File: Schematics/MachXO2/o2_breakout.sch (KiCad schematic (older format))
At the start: 34 parts, among them J1 Conn_02x20_Odd_Even, J2 Conn_02x20_Odd_Even, SW3 Reset, U1 LCMXO2-2000HC-4TG100C, U3 TCM809, U5 CY7C1010, U8 74AHC1G08, X1 19.6608MHz

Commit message: Update Schematic
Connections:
- wire segments 361 -> 363
- no-connect marks 28 -> 27
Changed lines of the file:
@@
 	10500 4250 10700 4250
 Wire Wire Line
-	10500 5550 10750 5550
+	10500 5450 10750 5450
 Text Label 10700 4250 2    50   ~ 0
 clkE
@@
 Text Label 5600 6400 2    50   ~ 0
 ~RTS
-Text Label 10750 5550 2    50   ~ 0
+Text Label 10750 5450 2    50   ~ 0
 GCLK1
 Text Label 5600 5200 2    50   ~ 0
@@
 Wire Wire Line
 	9700 5650 10000 5650
-Wire Wire Line
-	10500 5650 10800 5650
-Text Label 10800 5650 2    50   ~ 0
+Text Label 11050 5650 2    50   ~ 0
 SPI_CS3
 NoConn ~ 10000 5750
@@
 NoConn ~ 10500 5250
 NoConn ~ 10500 5350
-NoConn ~ 10500 5450
 NoConn ~ 10500 5750
 NoConn ~ 10000 1850
@@
 Wire Wire Line
 	9650 5950 9650 5050
-Wire Wire Line
-	10500 5950 10700 5950
 Wire Wire Line
 	10700 5950 10700 6050
@@
 L power:+5V #PWR?
 U 1 1 6089F76D
-P 10900 5750
+P 10900 5800
 AR Path="/5E6A6650/6089F76D" Ref="#PWR?"  Part="1"
 AR Path="/6089F76D" Ref="#PWR0107"  Part="1"
-F 0 "#PWR0107" H 10900 5600 50  0001 C CNN
-F 1 "+5V" H 10915 5923 50  0000 C CNN
-F 2 "" H 10900 5750 50  0001 C CNN
-F 3 "" H 10900 5750 50  0001 C CNN
-	1    10900 5750
-	1    0    0    -1
-$EndComp
-Wire Wire Line
-	10900 5750 10900 5850
+F 0 "#PWR0107" H 10900 5650 50  0001 C CNN
+F 1 "+5V" H 11000 5900 50  0000 C CNN
+F 2 "" H 10900 5800 50  0001 C CNN
+F 3 "" H 10900 5800 50  0001 C CNN
+	1    10900 5800
+	1    0    0    -1
+$EndComp
+Wire Wire Line
+	10900 5800 10900 5850
 Wire Wire Line
 	10500 5850 10900 5850
@@
 	10500 4850 10700 4850
 Wire Wire Line
-	11050 4650 11050 6150
-Wire Wire Line
-	11050 6150 10700 6150
-Wire Wire Line
-	10500 4650 11050 4650
+	11100 4650 11100 6150
+Wire Wire Line
+	11100 6150 10700 6150
+Wire Wire Line
+	10500 4650 11100 4650
 Connection ~ 10700 6150
 Wire Wire Line
@@
 Text Label 5600 4900 2    50   ~ 0
 nCS2
+Wire Wire Line
+	10500 5550 10700 5550
+Wire Wire Line
+	10700 5550 10700 5950
+Wire Wire Line
+	10500 5950 10700 5950
+Connection ~ 10700 5950
+Wire Wire Line
+	10500 5650 11050 5650
 Wire Bus Line
 	8000 1200 8000 3100

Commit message: Add schematic Rev C3.
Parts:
- added R12: 10K, Capacitors_SMD:C_0402, symbol CPU2908CLocal:R
- SW3: symbol Switch:SW_DPST_x2 -> o2_breakout-rescue:SW_DPST_x2-Switch
- U1: symbol FPGA_Lattice:LCMXO2-2000HC-4TG100C -> o2_breakout-rescue:LCMXO2-2000HC-4TG100C-FPGA_Lattice
- X1: symbol Oscillator:SG-8002CA -> o2_breakout-rescue:SG-8002CA-Oscillator
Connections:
- net labels added: FT_Reset
- wire segments 363 -> 368
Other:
- moved on the sheet: U3
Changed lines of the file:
@@
 L power:GND #PWR09
 U 1 1 5DC5EC0E
-P 9150 2100
-F 0 "#PWR09" H 9150 1850 50  0001 C CNN
-F 1 "GND" H 9155 1927 50  0000 C CNN
-F 2 "" H 9150 2100 50  0001 C CNN
-F 3 "" H 9150 2100 50  0001 C CNN
-	1    9150 2100
-	1    0    0    -1
-$EndComp
-Wire Wire Line
-	9150 1950 9150 2000
+P 8850 2100
+F 0 "#PWR09" H 8850 1850 50  0001 C CNN
+F 1 "GND" H 8855 1927 50  0000 C CNN
+F 2 "" H 8850 2100 50  0001 C CNN
+F 3 "" H 8850 2100 50  0001 C CNN
+	1    8850 2100
+	1    0    0    -1
+$EndComp
+Wire Wire Line
+	8850 1950 8850 2000
 Wire Wire Line
 	9650 6050 9650 6150
 $Comp
-L Oscillator:SG-8002CA X1
+L o2_breakout-rescue:SG-8002CA-Oscillator X1
 U 1 1 5DCCEBCB
 P 6450 5800
@@
 L Power_Supervisor:TCM809 U3
 U 1 1 5DC41577
-P 9250 1550
-F 0 "U3" H 9020 1596 50  0000 R CNN
-F 1 "TCM809" H 9020 1505 50  0000 R CNN
-F 2 "digikey-footprints:SOT-23-3" H 8850 1700 50  0001 C CNN
-F 3 "http://ww1.microchip.com/downloads/en/DeviceDoc/21661E.pdf" H 8950 1800 50  0001 C CNN
-	1    9250 1550
+P 8950 1550
+F 0 "U3" H 8720 1596 50  0000 R CNN
+F 1 "TCM809" H 8720 1505 50  0000 R CNN
+F 2 "digikey-footprints:SOT-23-3" H 8550 1700 50  0001 C CNN
+F 3 "http://ww1.microchip.com/downloads/en/DeviceDoc/21661E.pdf" H 8650 1800 50  0001 C CNN
+	1    8950 1550
 	1    0    0    -1
 $EndComp
@@
 $EndComp
 $Comp
-L power:+3V6 #PWR?
+L o2_breakout-rescue:+3V6-power #PWR?
 U 1 1 5DE300A4
 P 9350 900
@@
 Text Label 10500 1450 2    50   ~ 0
 nReset
-Text Label 8950 4850 0    50   ~ 0
-nReset
-Wire Wire Line
-	8950 4850 8850 4850
 $Comp
 L sram:CY7C1010 U5
@@
 Connection ~ 5850 7050
 $Comp
-L Switch:SW_DPST_x2 SW3
+L o2_breakout-rescue:SW_DPST_x2-Switch SW3
 U 1 1 5DEE7A37
 P 8250 1300
@@
 SPI_CLK
 Wire Wire Line
-	9950 1350 9950 1100
+	9950 1350 9950 1150
 Text Label 1800 4100 0    50   ~ 0
 clkE
@@
 	2150 4700 2150 5800
 $Comp
-L FPGA_Lattice:LCMXO2-2000HC-4TG100C U1
+L o2_breakout-rescue:LCMXO2-2000HC-4TG100C-FPGA_Lattice U1
 U 1 1 5DC03110
 P 2300 1500
@@
 	8250 1100 8500 1100
 Wire Wire Line
-	9550 1550 9600 1550
-Wire Wire Line
 	9600 1400 9600 1550
 Wire Wire Line
-	8500 700  9150 700
-Wire Wire Line
-	9150 700  9150 1150
+	8500 700  8850 700
+Wire Wire Line
+	8850 700  8850 1150
 Connection ~ 8500 700
-Wire Wire Line
-	8500 2000 9150 2000
-Connection ~ 9150 2000
-Wire Wire Line
-	9150 2000 9150 2100
+Connection ~ 8850 2000
+Wire Wire Line
+	8850 2000 8850 2100
 Connection ~ 6200 7050
 Connection ~ 6200 7500
@@
 Wire Wire Line
 	10500 5650 11050 5650
+Wire Wire Line
+	8500 2000 8850 2000
+Wire Wire Line
+	9250 1550 9350 1550
+Text Label 9300 1550 0    50   ~ 0
+FT_Reset
+Text Label 9350 4850 2    50   ~ 0
+FT_Reset
+Wire Wire Line
+	8850 4850 9350 4850
+$Comp
+L CPU2908CLocal:R R?
+U 1 1 5E34444C
+P 9350 1350
+AR Path="/5E6A6650/5E34444C" Ref="R?"  Part="1"
+AR Path="/5E34444C" Ref="R12"  Part="1"
+F 0 "R12" H 9420 1396 50  0000 L CNN
+F 1 "10K" H 9420 1305 50  0000 L CNN
+F 2 "Capacitors_SMD:C_0402" V 9280 1350 50  0001 C CNN
+F 3 "~" H 9350 1350 50  0001 C CNN
+	1    9350 1350
+	1    0    0    -1
+$EndComp
+Wire Wire Line
+	9350 1500 9350 1550
+Connection ~ 9350 1550
+Wire Wire Line
+	9350 1550 9600 1550
+Wire Wire Line
+	9350 1200 9350 1150
+Wire Wire Line
+	9350 1150 9950 1150
 Wire Bus Line
 	8000 1200 8000 3100
@@
 Wire Bus Line
 	6050 1100 6050 3500
+Connection ~ 9950 1150
+Wire Wire Line
+	9950 1150 9950 1100
 $EndSCHEMATC

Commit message: Update BreakOut Schematic.
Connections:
- net +3V3: no longer J1.2 (Pin_2)
- net GND: now also J1.2 (Pin_2), J1.20 (Pin_20)
- net ~SD_CD: now also U1.62 (PR7B)
- no-connect marks 27 -> 24
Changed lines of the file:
@@
 UM4
 Wire Wire Line
-	10950 5150 10950 4150
-Wire Wire Line
 	10950 2850 10950 3950
-Connection ~ 10950 4150
 Wire Wire Line
 	10950 1850 10950 2750
@@
 Wire Wire Line
 	10500 2850 10950 2850
-Wire Wire Line
-	10500 4150 10950 4150
 Wire Wire Line
 	10500 5150 10950 5150
@@
 NoConn ~ 10500 5350
 NoConn ~ 10500 5750
-NoConn ~ 10000 1850
 NoConn ~ 10000 2050
 NoConn ~ 10000 2150
@@
 Wire Wire Line
 	10850 3750 10850 3650
-NoConn ~ 10500 5050
 NoConn ~ 2300 3500
 NoConn ~ 2300 3100
@@
 NoConn ~ 2300 4300
 NoConn ~ 5100 4800
-NoConn ~ 5100 5300
 NoConn ~ 2300 5700
 NoConn ~ 2300 5900
@@
 Connection ~ 10950 3950
 Wire Wire Line
-	10950 3950 10950 4150
-Wire Wire Line
 	10000 1850 9850 1850
 Wire Wire Line
@@
 	10500 4850 10700 4850
 Wire Wire Line
-	11100 4650 11100 6150
+	11100 4650 11100 5050
 Wire Wire Line
 	11100 6150 10700 6150
@@
 Wire Wire Line
 	9250 1550 9350 1550
-Text Label 9300 1550 0    50   ~ 0
+Text Label 9700 1700 2    50   ~ 0
 FT_Reset
 Text Label 9350 4850 2    50   ~ 0
@@
 Wire Wire Line
 	9350 1150 9950 1150
+Connection ~ 9950 1150
+Wire Wire Line
+	9950 1150 9950 1100
+Wire Wire Line
+	9350 1550 9350 1700
+Wire Wire Line
+	9350 1700 9700 1700
+Wire Wire Line
+	5100 5300 5600 5300
+Text Label 5600 5300 2    50   ~ 0
+~SD_CD
+Wire Wire Line
+	10950 3950 10950 5150
+Wire Wire Line
+	10500 4150 11100 4150
+Wire Wire Line
+	11100 4150 11100 4650
+Connection ~ 11100 4650
+Wire Wire Line
+	10500 5050 11100 5050
 Wire Bus Line
 	8000 1200 8000 3100
@@
 Wire Bus Line
 	6050 1100 6050 3500
-Connection ~ 9950 1150
-Wire Wire Line
-	9950 1150 9950 1100
+Connection ~ 11100 5050
+Wire Wire Line
+	11100 5050 11100 6150
 $EndSCHEMATC

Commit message: Update Schematics
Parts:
- added C38: 0.1uF, Capacitors_SMD:C_0402, symbol Device:C
- added R26: 10K, Capacitors_SMD:C_0402, symbol CPU2908CLocal:R
- added SW1: USER, Buttons_Switches_ThroughHole:SW_PUSH_6mm, symbol o2_breakout-rescue:SW_DPST_x2-Switch
- added unit 1 of SW2
- renumbered SW3 to SW2
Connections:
- net +3V3: now also R26.1; no longer J2.20 (Pin_20), J2.22 (Pin_22)
- net A0: now also J2.8 (Pin_8); no longer J2.10 (Pin_10)
- net A1: now also J2.7 (Pin_7); no longer J2.9 (Pin_9)
- net A10: now also J2.20 (Pin_20); no longer J2.26 (Pin_26)
- net A11: now also J2.19 (Pin_19); no longer J2.25 (Pin_25)
- net A12: now also J2.22 (Pin_22); no longer J2.28 (Pin_28)
- net A13: now also J2.21 (Pin_21); no longer J2.27 (Pin_27)
- net A14: now also J2.24 (Pin_24); no longer J2.30 (Pin_30)
- net A15: now also J2.23 (Pin_23); no longer J2.29 (Pin_29)
- net A16: now also J2.28 (Pin_28); no longer J2.32 (Pin_32)
- net A17: now also J2.27 (Pin_27); no longer J2.31 (Pin_31)
- net A18: now also J2.30 (Pin_30); no longer J2.34 (Pin_34)
- net A19: now also J2.29 (Pin_29); no longer J2.33 (Pin_33)
- net A2: now also J2.10 (Pin_10); no longer J2.12 (Pin_12)
- net A3: now also J2.9 (Pin_9); no longer J2.11 (Pin_11)
- net A4: now also J2.12 (Pin_12); no longer J2.14 (Pin_14)
- net A5: now also J2.11 (Pin_11); no longer J2.13 (Pin_13)
- net A6: now also J2.14 (Pin_14); no longer J2.16 (Pin_16)
- net A7: now also J2.13 (Pin_13); no longer J2.15 (Pin_15)
- net A8: now also J2.18 (Pin_18); no longer J2.24 (Pin_24)
- net A9: now also J2.17 (Pin_17); no longer J2.23 (Pin_23)
- net GND: now also J1.13 (Pin_13), J1.14 (Pin_14), J2.15 (Pin_15), J2.16 (Pin_16), J2.25 (Pin_25), J2.26 (Pin_26), J2.31 (Pin_31), J2.32 (Pin_32), SW2.4 (B), C38.2, SW1.1 (A), SW1.4 (B), SW2.1 (A); no longer J1.12 (Pin_12), J1.19 (Pin_19), J1.20 (Pin_20), J2.19 (Pin_19), J2.21 (Pin_21), J2.37 (Pin_37), J2.38 (Pin_38), J2.39 (Pin_39), J2.40 (Pin_40), SW2.1 (A)
- net IO0: now also J2.34 (Pin_34)
- net IO1: now also J2.33 (Pin_33)
- net IO2: now also J2.36 (Pin_36)
- net IO3: now also J2.35 (Pin_35)
- net IO4: now also J2.38 (Pin_38)
- net IO5: now also J2.37 (Pin_37)
- net IO6: now also J2.40 (Pin_40)
- net IO7: now also J2.39 (Pin_39)
- net ~SD_CD: now also J2.5 (Pin_5); no longer J2.8 (Pin_8)
- net ~nAltRD: now also J1.20 (Pin_20); no longer J1.17 (Pin_17)
- net ~nAltWR: now also J1.19 (Pin_19); no longer J1.18 (Pin_18)
- net USER: now reaches U1.15 (PL9B)
- net USER: now also C38.1, R26.2, SW1.3 (A)
- net ~CS1: now reaches U1.29 (PB6A)
- net ~CS1: now also J1.8 (Pin_8)
- net at C26.1, U8.2: now also SW2.3 (A); no longer R10.2, SW2.2 (B)
- net UM0 renamed IO8
- net IO8: now also J1.10 (Pin_10); no longer J1.8 (Pin_8)
- net UM1 renamed IO9
- net UM2 renamed IO10
- net IO10: now also J1.12 (Pin_12); no longer J1.10 (Pin_10)
- net UM3 renamed IO11
- net UM4 renamed IO12
- net IO12: now also J1.16 (Pin_16); no longer J1.13 (Pin_13)
- net UM5 renamed IO13
- net IO13: now also J1.15 (Pin_15); no longer J1.14 (Pin_14)
- net UM6 renamed IO14
- net IO14: now also J1.18 (Pin_18); no longer J1.15 (Pin_15)
- net UM7 renamed IO15
- net IO15: now also J1.17 (Pin_17); no longer J1.16 (Pin_16)
- net nCS0 renamed ~CE
- net nCS2 renamed ~CS2
- new net: R10.2, SW2.2 (B)
- no-connect marks 24 -> 17

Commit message: Update schematics
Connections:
- net GND: now also J1.23 (Pin_23), J1.24 (Pin_24)
- no-connect marks 17 -> 15
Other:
- moved on the sheet: C38
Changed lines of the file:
@@
 NoConn ~ 10000 5450
 NoConn ~ 10000 5350
-NoConn ~ 10000 5250
-NoConn ~ 10500 5250
 NoConn ~ 10500 5350
 NoConn ~ 10500 5750
@@
 	10500 4150 11100 4150
 Wire Wire Line
-	7300 4700 7350 4700
+	7300 4700 7450 4700
 $Comp
 L CPU2908CLocal:R R?
@@
 	7200 5250 7200 5350
 Wire Wire Line
-	7350 5250 7200 5250
+	7450 5250 7200 5250
 $Comp
 L o2_breakout-rescue:SW_DPST_x2-Switch SW1
@@
 Connection ~ 9650 4750
 Wire Wire Line
-	9650 4750 9650 5950
+	9650 4750 9650 5250
 Wire Wire Line
 	10950 3950 10950 5150
@@
 Connection ~ 11100 4750
 Wire Wire Line
-	11100 4750 11100 6150
+	11100 4750 11100 5250
 $Comp
 L Connector_Generic:Conn_02x20_Odd_Even J1
@@
 	10500 4450 10700 4450
 Wire Wire Line
-	7350 5150 7350 5250
+	7450 5150 7450 5250
 $Comp
 L Device:C C38
 U 1 1 5E3FD7EE
-P 7350 5000
-F 0 "C38" H 7465 5046 50  0000 L CNN
-F 1 "0.1uF" H 7465 4955 50  0000 L CNN
-F 2 "Capacitors_SMD:C_0402" H 7388 4850 50  0001 C CNN
-F 3 "~" H 7350 5000 50  0001 C CNN
-	1    7350 5000
-	1    0    0    -1
-$EndComp
-Wire Wire Line
-	7350 4700 7350 4850
-Connection ~ 7350 4700
+P 7450 5000
+F 0 "C38" H 7565 5046 50  0000 L CNN
+F 1 "0.1uF" H 7565 4955 50  0000 L CNN
+F 2 "Capacitors_SMD:C_0402" H 7488 4850 50  0001 C CNN
+F 3 "~" H 7450 5000 50  0001 C CNN
+	1    7450 5000
+	1    0    0    -1
+$EndComp
+Wire Wire Line
+	7450 4700 7450 4850
 Text Label 1800 2900 0    50   ~ 0
 USER
 Wire Wire Line
-	7350 4700 7650 4700
-Wire Wire Line
 	1800 2900 2300 2900
+Text Label 6900 4700 0    50   ~ 0
+USER
+Wire Wire Line
+	9650 5250 10000 5250
+Connection ~ 9650 5250
+Wire Wire Line
+	9650 5250 9650 5950
+Wire Wire Line
+	10500 5250 11100 5250
+Connection ~ 11100 5250
+Wire Wire Line
+	11100 5250 11100 6150
+Wire Wire Line
+	6900 4700 7200 4700
+Connection ~ 7200 4700
 Wire Bus Line
 	8000 1200 8000 3100
@@
 Wire Bus Line
 	6050 1100 6050 3500
-Text Label 7650 4700 2    50   ~ 0
-USER
 $EndSCHEMATC

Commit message: Clean up PCB.
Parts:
- removed C26: 0.1uF, Capacitors_SMD:C_0402, symbol Device:C
- added C39: 0.1uF, Capacitors_SMD:C_0402, symbol Device:C
- JP2: footprint Wire_Connections_Bridges:WireConnection_0.80mmDrill -> Wire_Connections_Bridges:WireConnection_1.00mmDrill
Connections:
- net +3V3: now also J1.33 (Pin_33), J1.34 (Pin_34)
- net GND: now also C39.2; no longer J1.37 (Pin_37), J1.38 (Pin_38)
- net at R10.2, SW2.2 (B): now also C39.1
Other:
- moved on the sheet: C1, C2, C3, C35, C4, C5, C6, C7, R10, SW2A

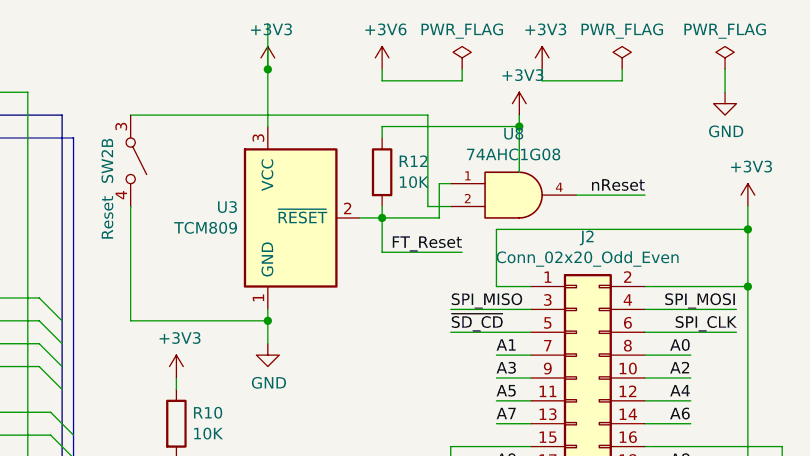
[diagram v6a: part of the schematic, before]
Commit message: asq bug fix.
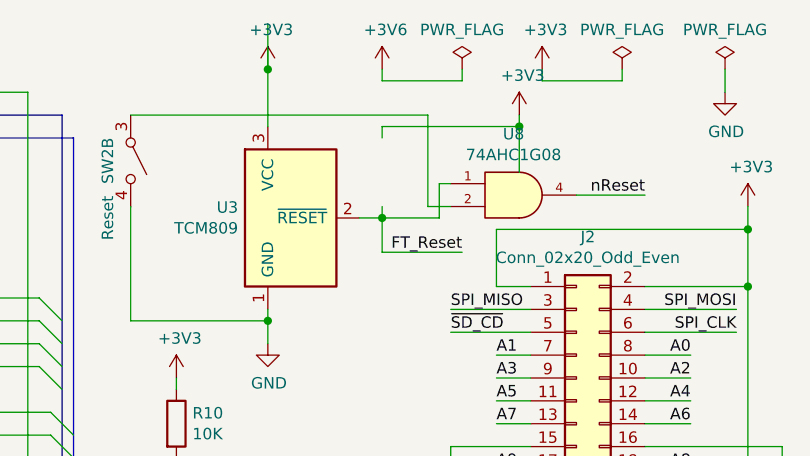
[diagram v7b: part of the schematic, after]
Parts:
- removed R12: 10K, Capacitors_SMD:C_0402, symbol CPU2908CLocal:R
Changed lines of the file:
@@
 Wire Wire Line
 	8850 4850 9350 4850
-$Comp
-L CPU2908CLocal:R R?
-U 1 1 5E34444C
-P 9350 1350
-AR Path="/5E6A6650/5E34444C" Ref="R?"  Part="1"
-AR Path="/5E34444C" Ref="R12"  Part="1"
-F 0 "R12" H 9420 1396 50  0000 L CNN
-F 1 "10K" H 9420 1305 50  0000 L CNN
-F 2 "Capacitors_SMD:C_0402" V 9280 1350 50  0001 C CNN
-F 3 "~" H 9350 1350 50  0001 C CNN
-	1    9350 1350
-	1    0    0    -1
-$EndComp
 Wire Wire Line
 	9350 1500 9350 1550

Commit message: PCB RevA3.
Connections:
- net GND: now also J1.29 (Pin_29)
- net SPI_CS0: now also U1.62 (PR7B); no longer U1.61 (PR9A)
- net ~CS2: now also J1.27 (Pin_27)
- net ~SD_CD: now also U1.61 (PR9A); no longer U1.62 (PR7B)
- no-connect marks 15 -> 13
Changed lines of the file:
@@
 Text Label 5600 5200 2    50   ~ 0
 GCLK1
-Text Label 5600 5100 2    50   ~ 0
-~CS0
 Text Label 5600 5500 2    50   ~ 0
 SPI_CS1
-Text Label 5600 5400 2    50   ~ 0
+Text Label 5600 5300 2    50   ~ 0
 SPI_CS0
 Wire Wire Line
@@
 Text Label 11050 5650 2    50   ~ 0
 SPI_CS3
-NoConn ~ 10000 5550
-NoConn ~ 10000 5450
 NoConn ~ 10000 5350
 NoConn ~ 10500 5350
@@
 Wire Wire Line
 	5100 5300 5600 5300
-Text Label 5600 5300 2    50   ~ 0
-~SD_CD
 Wire Wire Line
 	10500 4150 11100 4150
@@
 	10700 5550 10700 6050
 Wire Wire Line
-	9650 5250 9650 6050
+	9650 5250 9650 5550
 NoConn ~ 10000 5950
 NoConn ~ 10500 5950
+Text Label 9700 5450 0    50   ~ 0
+~CS2
+Wire Wire Line
+	9700 5450 10000 5450
+Wire Wire Line
+	10000 5550 9650 5550
+Connection ~ 9650 5550
+Wire Wire Line
+	9650 5550 9650 6050
 Wire Bus Line
 	8000 1200 8000 3100
@@
 Wire Bus Line
 	6050 1100 6050 3500
+Text Label 5600 5100 2    50   ~ 0
+~CS0
+Text Label 5600 5400 2    50   ~ 0
+~SD_CD
 $EndSCHEMATC
